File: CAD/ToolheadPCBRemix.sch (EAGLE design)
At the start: 16 parts

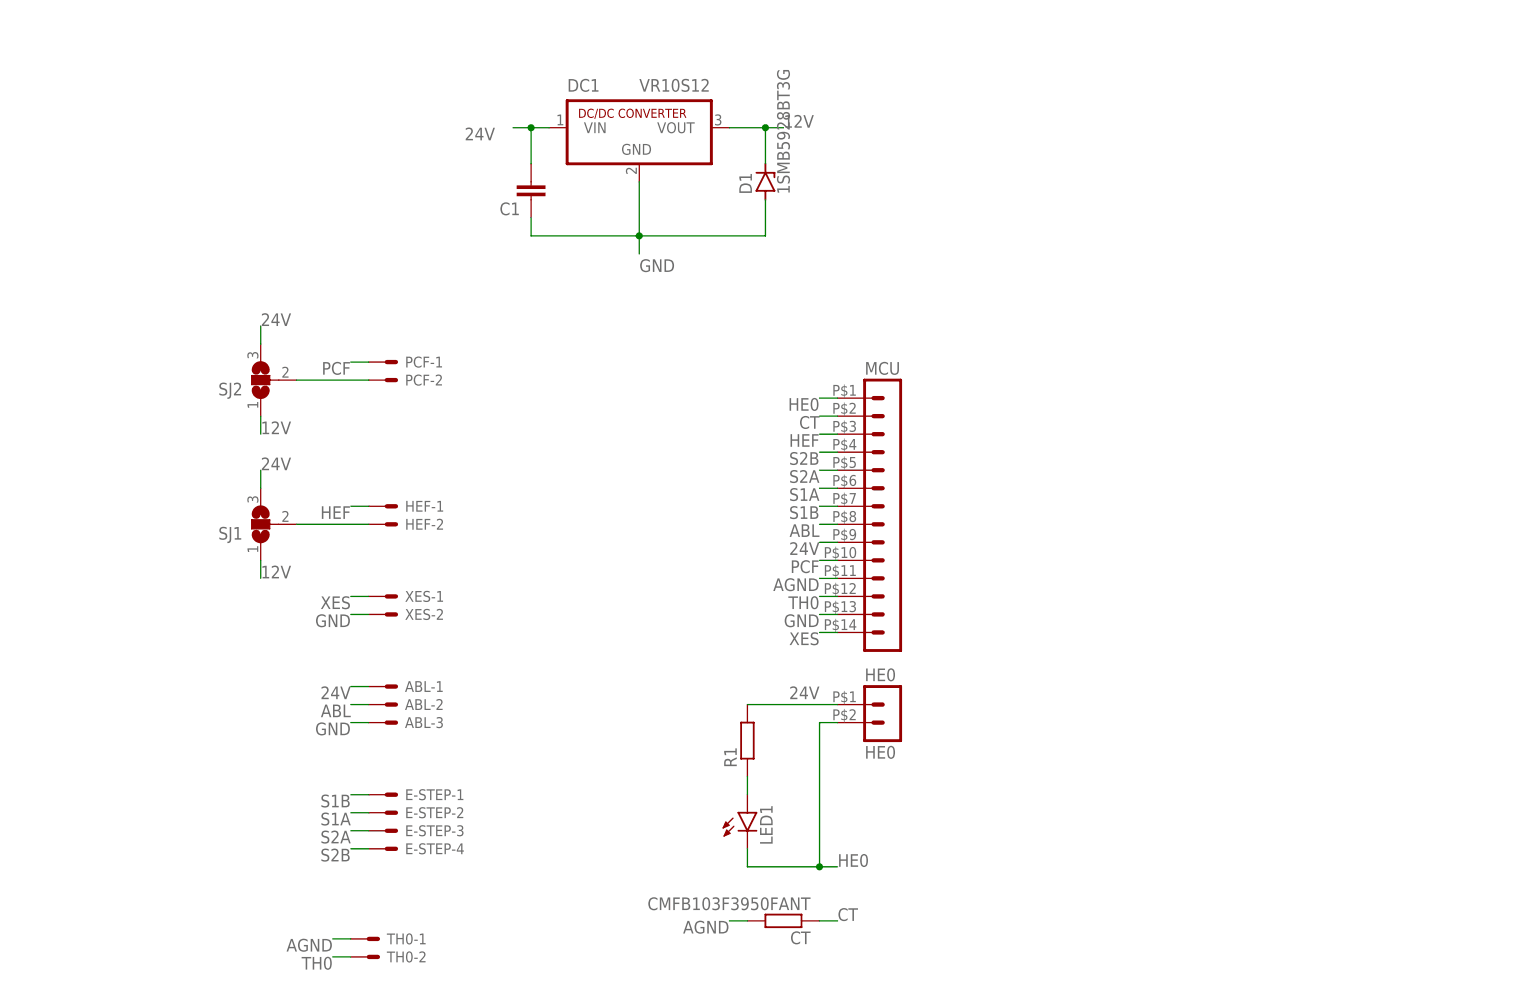
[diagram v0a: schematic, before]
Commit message: Update to dual vregs (12V/5V)
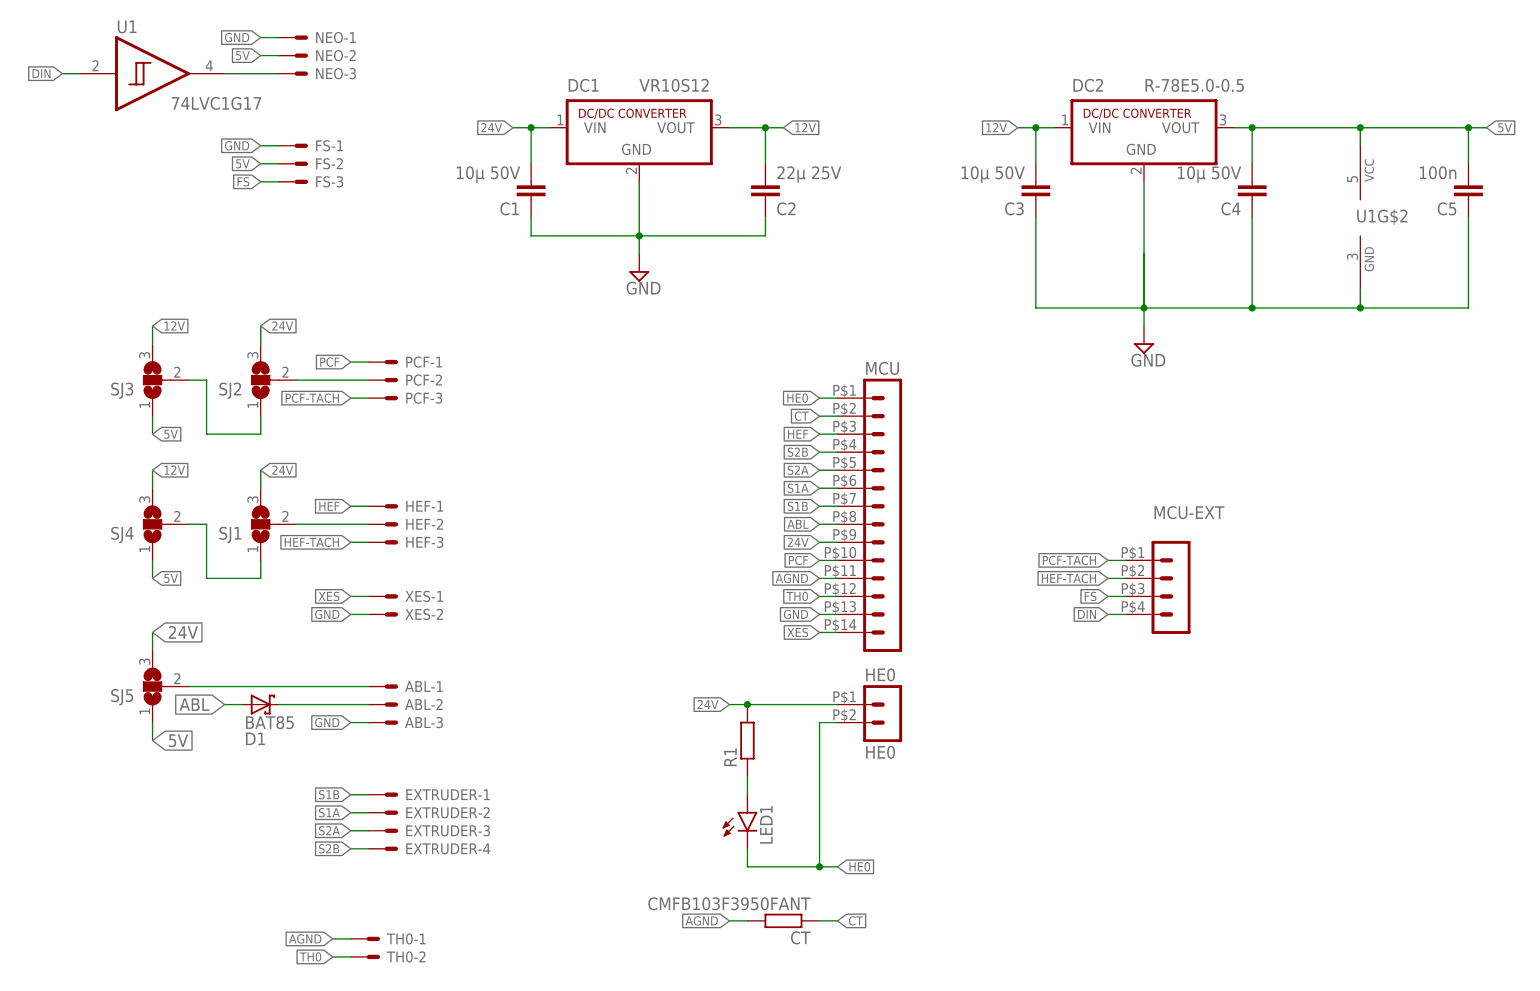
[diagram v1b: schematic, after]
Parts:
- added C2: 22µ 25V, rcl:C-EUC1206
- added C3, C4: 10µ 50V, rcl:C-EUC1206
- added C5: 100n, rcl:C-EUC0805
- added DC2: R-78E5.0-0.5, dc-dc-converter:R-78C5.0-1.0
- added FS, NEO: JST-XH-03-PIN-ROUND-PAD, Rembrandt Electronics - JST XH Connectors v1-0:JST-XH-03-PIN-ROUND-PAD
- added MCU-EXT: (no value), con-molex-micro-fit-3_0:HEADER_POS4_43045-0401
- added SJ3, SJ4, SJ5: (no value), jumper:SJ2W
- added U1: 74LVC1G17, logick:74LVC1G17
- C1: value (none) -> 10µ 50V
- D1: value 1SMB5928BT3G -> BAT85; device diode:ZENER-DIODESMB -> nxp_60_1_1:BAT85
- HEF, PCF: value JST-XH-02-PIN-ROUND-PAD -> JST-XH-03-PIN-ROUND-PAD; device Rembrandt Electronics - JST XH Connectors v1-0:JST-XH-02-PIN-ROUND-PAD -> Rembrandt Electronics - JST XH Connectors v1-0:JST-XH-03-PIN-ROUND-PAD
- renumbered E-STEP to EXTRUDER
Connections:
- new net 5V: C4.2, C5.2, DC2.VOUT, FS-2.S, NEO-2.S, SJ3.1, SJ4.1, SJ5.1, U1G$2.VCC
- new net DIN: MCU-EXT.4, U1G$1.A
- new net FS: FS-3.S, MCU-EXT.3
- new net HEF-TACH: HEF-3.S, MCU-EXT.2
- new net N$10: ABL-2.S, D1.K
- new net N$4: NEO-3.S, U1G$1.Y
- new net N$5: SJ2.1, SJ3.2
- new net N$8: SJ1.1, SJ4.2
- new net N$9: ABL-1.S, SJ5.2
- new net PCF-TACH: MCU-EXT.1, PCF-3.S
- net 12V: now also C2.2, C3.2, DC2.VIN, SJ3.3, SJ4.3; no longer D1.C, SJ1.1, SJ2.1
- net 24V: now also SJ5.3; no longer ABL-1.S
- net ABL: now also D1.A; no longer ABL-2.S
- net GND: now also C2.1, C3.1, C4.1, C5.1, DC2.GND, FS-1.S, NEO-1.S, U1G$2.GND; no longer D1.A
